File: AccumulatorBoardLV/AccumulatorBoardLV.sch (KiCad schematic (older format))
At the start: 39 parts, among them J1 BMS Connector 1, J10 Contactor 2, J11 IMD LV, J12 Temperature Board, J13 Energy Meter, J14 Energy Meter, J15 12V from DCDC, J16 HV Interlock, J18 Charger LV, J19 Lid Interlock, J2 BMS Connector 2, J3 BMS TX, J4 BMS RX, J5 BMS Reset, J7 IMD Reset, J8 Temp Reset, J9 Contactor 1, P3 Charger Interlock, U13 DK1A1B-12V, U14 DK1A1B-12V, U15 DK1A1B-12V, U17 G5RL-K1A-E, U18 G5RL-K1A-E, U19 G5RL-K1A-E, U6 L78S05CV-DG, U8 LM555N

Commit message: Clean up LV accumulator schematic
Need to solidify connections between accumulator LV board and temp board
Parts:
- removed J12: Temperature Board, symbol CONN_01X06
- added J?: Current Sensor, symbol CONN_01X03
- added P?: To Temp Board, symbol CONN_01X08
- J?: renamed from P?; value CONN_01X14 -> To ECU
- renumbered P3 to J?
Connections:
- net labels added: AIRS_FINAL_CHARGER
- net labels removed: AIRS_LID_OUT, CUR_SIG
- no-connect marks 2 -> 3
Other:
- moved on the sheet: C1, C?, H1, R10, R11, R12, R8, R9, U13, U14, U15, U6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

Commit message: Add connections to temp board for isolation and fault feedback
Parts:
- removed R10: 2.5kR, symbol R
- removed R8: 3.5kR, symbol R
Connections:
- net labels added: BMS_FLT_LATCHED, IMD_FLT_LATCHED, TEMP_FLT_LATCHED
- wire segments 28 -> 30
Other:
- moved on the sheet: C?, U6
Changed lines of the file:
@@
 LIBS:valves
 LIBS:arduino
-LIBS:AccumulatorBoardLV-cache
 EELAYER 25 0
 EELAYER END
@@
 L L78S05CV-DG U6
 U 1 1 58ABDAE7
-P 2900 6900
-F 0 "U6" H 2700 6800 50  0000 C CNN
-F 1 "L78S05CV-DG" H 2650 7100 50  0000 L CNN
-F 2 "Power_Integrations:TO-220" H 2900 6550 50  0001 C CIN
-F 3 "" H 2900 6900 50  0000 C CNN
-	1    2900 6900
-	1    0    0    -1
-$EndComp
-Text Label 2900 7150 3    60   ~ 0
+P 2800 5600
+F 0 "U6" H 2600 5500 50  0000 C CNN
+F 1 "L78S05CV-DG" H 2550 5800 50  0000 L CNN
+F 2 "Power_Integrations:TO-220" H 2800 5250 50  0001 C CIN
+F 3 "" H 2800 5600 50  0000 C CNN
+	1    2800 5600
+	1    0    0    -1
+$EndComp
+Text Label 2800 5850 3    60   ~ 0
 GND
 $Comp
@@
 L +5V #PWR02
 U 1 1 58B23863
-P 3300 6850
-F 0 "#PWR02" H 3300 6700 50  0001 C CNN
-F 1 "+5V" H 3300 6990 50  0000 C CNN
-F 2 "" H 3300 6850 50  0000 C CNN
-F 3 "" H 3300 6850 50  0000 C CNN
-	1    3300 6850
+P 3200 5550
+F 0 "#PWR02" H 3200 5400 50  0001 C CNN
+F 1 "+5V" H 3200 5690 50  0000 C CNN
+F 2 "" H 3200 5550 50  0000 C CNN
+F 3 "" H 3200 5550 50  0000 C CNN
+	1    3200 5550
 	1    0    0    -1
 $EndComp
@@
 L +12V #PWR017
 U 1 1 58B2EAED
-P 2500 6850
-F 0 "#PWR017" H 2500 6700 50  0001 C CNN
-F 1 "+12V" H 2500 6990 50  0000 C CNN
-F 2 "" H 2500 6850 50  0000 C CNN
-F 3 "" H 2500 6850 50  0000 C CNN
-	1    2500 6850
+P 2400 5550
+F 0 "#PWR017" H 2400 5400 50  0001 C CNN
+F 1 "+12V" H 2400 5690 50  0000 C CNN
+F 2 "" H 2400 5550 50  0000 C CNN
+F 3 "" H 2400 5550 50  0000 C CNN
+	1    2400 5550
 	1    0    0    -1
 $EndComp
@@
 Text Label 6400 3550 2    60   ~ 0
 TEMP_FLT
-Text Label 6900 1800 2    60   ~ 0
-BMS_FLT
 Text Label 6900 2100 2    60   ~ 0
 IMD_FLT
@@
 	1    0    0    -1
 $EndComp
-$Comp
-L R R8
-U 1 1 58B6CCA1
-P 7050 1800
-F 0 "R8" V 7130 1800 50  0000 C CNN
-F 1 "3.5kR" V 7050 1800 50  0000 C CNN
-F 2 "" V 6980 1800 50  0001 C CNN
-F 3 "" H 7050 1800 50  0000 C CNN
-	1    7050 1800
-	0    1    1    0
-$EndComp
-$Comp
-L R R10
-U 1 1 58B6D248
-P 7200 1650
-F 0 "R10" V 7280 1650 50  0000 C CNN
-F 1 "2.5kR" V 7200 1650 50  0000 C CNN
-F 2 "" V 7130 1650 50  0001 C CNN
-F 3 "" H 7200 1650 50  0000 C CNN
-	1    7200 1650
-	1    0    0    -1
-$EndComp
-$Comp
-L GND #PWR035
-U 1 1 58B6D770
-P 7200 1500
-F 0 "#PWR035" H 7200 1250 50  0001 C CNN
-F 1 "GND" H 7200 1350 50  0000 C CNN
-F 2 "" H 7200 1500 50  0000 C CNN
-F 3 "" H 7200 1500 50  0000 C CNN
-	1    7200 1500
-	0    -1   -1   0
-$EndComp
 Text Label 9450 5150 2    60   ~ 0
 IMD_FLT_H
@@
 NoConn ~ 1100 2400
 Wire Wire Line
-	7200 1800 7500 1800
-Wire Wire Line
 	7200 2100 7500 2100
-Text Label 7500 1800 0    60   ~ 0
-BMS_FLT_5
 Text Label 7500 2100 0    60   ~ 0
 IMD_FLT_5
@@
 L GND #PWR?
 U 1 1 595AA8FC
-P 2500 7150
-F 0 "#PWR?" H 2500 6900 50  0001 C CNN
-F 1 "GND" H 2500 7000 50  0000 C CNN
-F 2 "" H 2500 7150 50  0001 C CNN
-F 3 "" H 2500 7150 50  0001 C CNN
-	1    2500 7150
+P 2400 5850
+F 0 "#PWR?" H 2400 5600 50  0001 C CNN
+F 1 "GND" H 2400 5700 50  0000 C CNN
+F 2 "" H 2400 5850 50  0001 C CNN
+F 3 "" H 2400 5850 50  0001 C CNN
+	1    2400 5850
 	1    0    0    -1
 $EndComp
@@
 L CP C?
 U 1 1 595AB32A
-P 3300 7000
-F 0 "C?" H 3325 7100 50  0000 L CNN
-F 1 "0.1uF" H 3325 6900 50  0000 L CNN
-F 2 "" H 3338 6850 50  0001 C CNN
-F 3 "" H 3300 7000 50  0001 C CNN
-	1    3300 7000
+P 3200 5700
+F 0 "C?" H 3225 5800 50  0000 L CNN
+F 1 "0.1uF" H 3225 5600 50  0000 L CNN
+F 2 "" H 3238 5550 50  0001 C CNN
+F 3 "" H 3200 5700 50  0001 C CNN
+	1    3200 5700
 	1    0    0    -1
 $EndComp
@@
 L C C?
 U 1 1 595AB43E
-P 2500 7000
-F 0 "C?" H 2525 7100 50  0000 L CNN
-F 1 "0.47uF" H 2525 6900 50  0000 L CNN
-F 2 "" H 2538 6850 50  0001 C CNN
-F 3 "" H 2500 7000 50  0001 C CNN
-	1    2500 7000
+P 2400 5700
+F 0 "C?" H 2425 5800 50  0000 L CNN
+F 1 "0.47uF" H 2425 5600 50  0000 L CNN
+F 2 "" H 2438 5550 50  0001 C CNN
+F 3 "" H 2400 5700 50  0001 C CNN
+	1    2400 5700
 	1    0    0    -1
 $EndComp
@@
 L GND #PWR?
 U 1 1 595AB92B
-P 3300 7150
-F 0 "#PWR?" H 3300 6900 50  0001 C CNN
-F 1 "GND" H 3300 7000 50  0000 C CNN
-F 2 "" H 3300 7150 50  0001 C CNN
-F 3 "" H 3300 7150 50  0001 C CNN
-	1    3300 7150
+P 3200 5850
+F 0 "#PWR?" H 3200 5600 50  0001 C CNN
+F 1 "GND" H 3200 5700 50  0000 C CNN
+F 2 "" H 3200 5850 50  0001 C CNN
+F 3 "" H 3200 5850 50  0001 C CNN
+	1    3200 5850
 	1    0    0    -1
 $EndComp
@@
 5V_BMS
 Wire Wire Line
-	2500 7150 3300 7150
-Connection ~ 2900 7150
+	2400 5850 3200 5850
+Connection ~ 2800 5850
 Text Label 5050 1100 3    60   ~ 0
 SIG_CURRENT
@@
 NoConn ~ 1100 3350
 NoConn ~ -1800 4150
+$Comp
+L GND #PWR?
+U 1 1 59A4B84E
+P 10800 2100
+F 0 "#PWR?" H 10800 1850 50  0001 C CNN
+F 1 "GND" H 10800 1950 50  0000 C CNN
+F 2 "" H 10800 2100 50  0000 C CNN
+F 3 "" H 10800 2100 50  0000 C CNN
+	1    10800 2100
+	1    0    0    -1
+$EndComp
+$Comp
+L GND #PWR?
+U 1 1 59A4B8D4
+P 10800 3450
+F 0 "#PWR?" H 10800 3200 50  0001 C CNN
+F 1 "GND" H 10800 3300 50  0000 C CNN
+F 2 "" H 10800 3450 50  0000 C CNN
+F 3 "" H 10800 3450 50  0000 C CNN
+	1    10800 3450
+	1    0    0    -1
+$EndComp
+$Comp
+L GND #PWR?
+U 1 1 59A4B95A
+P 10800 4850
+F 0 "#PWR?" H 10800 4600 50  0001 C CNN
+F 1 "GND" H 10800 4700 50  0000 C CNN
+F 2 "" H 10800 4850 50  0000 C CNN
+F 3 "" H 10800 4850 50  0000 C CNN
+	1    10800 4850
+	1    0    0    -1
+$EndComp
+Text Label 10800 700  2    60   ~ 0
+BMS_FLT_LATCHED
+Text Label 10800 2550 2    60   ~ 0
+TEMP_FLT_LATCHED
+Text Label 10800 3950 2    60   ~ 0
+IMD_FLT_LATCHED
+Wire Wire Line
+	10800 1500 10800 700
+Wire Wire Line
+	10800 2850 10800 2550
+Wire Wire Line
+	10800 3950 10800 4250
 $EndSCHEMATC

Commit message: Progress on PE LV and HV boards
Upgraded to Kicad 4.0.7
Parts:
- J1, J13, J14: symbol CONN_01X04 -> Conn_01x04
- J10, J15, J16, J19, J3, J4, J5, J7, J8, J9, J?: symbol CONN_01X02 -> Conn_01x02
- J11: symbol CONN_01X06 -> Conn_01x06
- J18, P?: symbol CONN_01X08 -> Conn_01x08
- J2: symbol CONN_01X12 -> Conn_01x12
- J?: symbol CONN_01X14 -> Conn_01x14
- J?: symbol CONN_01X03 -> Conn_01x03

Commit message: Hopefully finalize PCB schematics
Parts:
- removed J13, J14: Energy Meter, symbol Conn_01x04
- removed J15: 12V from DCDC, Connectors_Molex:Molex_NanoFit_1x02x2.50mm_Straight, symbol Conn_01x02
- removed P?: To Temp Board, symbol Conn_01x08
- added J?: To HV Board, symbol Conn_01x03
- added J?: To Temp Board, symbol Conn_01x10
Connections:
- net labels removed: BMS_FLT_5, EM_COMM+, EM_COMM-
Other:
- moved on the sheet: J16, J?
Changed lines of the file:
@@
 L Conn_01x02 J16
 U 1 1 58A9F1D8
-P 900 5750
-F 0 "J16" H 900 5900 50  0000 C CNN
-F 1 "HV Interlock" V 1000 5750 50  0000 C CNN
-F 2 "Connectors_Molex:Molex_NanoFit_1x02x2.50mm_Straight" H 900 5750 50  0001 C CNN
-F 3 "" H 900 5750 50  0000 C CNN
-	1    900  5750
+P 900 4550
+F 0 "J16" H 900 4700 50  0000 C CNN
+F 1 "HV Interlock" V 1000 4550 50  0000 C CNN
+F 2 "Connectors_Molex:Molex_NanoFit_1x02x2.50mm_Straight" H 900 4550 50  0001 C CNN
+F 3 "" H 900 4550 50  0000 C CNN
+	1    900  4550
 	-1   0    0    -1
 $EndComp
-Text Label 1100 5850 0    60   ~ 0
+Text Label 1100 4650 0    60   ~ 0
 AIRS_FINAL_OUT
 $Comp
@@
 Text Label 8900 4300 2    60   ~ 0
 IMD_FLT_H
-$Comp
-L Conn_01x02 J15
-U 1 1 58B9D04E
-P 900 5050
-F 0 "J15" H 900 5200 50  0000 C CNN
-F 1 "12V from DCDC" V 1000 5050 50  0000 C CNN
-F 2 "Connectors_Molex:Molex_NanoFit_1x02x2.50mm_Straight" H 900 5050 50  0001 C CNN
-F 3 "" H 900 5050 50  0000 C CNN
-	1    900  5050
-	-1   0    0    -1
-$EndComp
-Text Label 1100 5050 0    60   ~ 0
+Text Label 1100 3850 0    60   ~ 0
 12V_SRC
-Text Label 1100 5150 0    60   ~ 0
+Text Label 1100 3950 0    60   ~ 0
 GND
 $Comp
@@
 Text Label 7400 6050 0    60   ~ 0
 TEMP_RESET
-Text Label 1100 2650 0    60   ~ 0
+Text Label 1100 2750 0    60   ~ 0
 5V
-Text Label 1100 2750 0    60   ~ 0
-GND
 Text Label 1100 2850 0    60   ~ 0
+GND
+Text Label 1100 2950 0    60   ~ 0
 CAN_H
-Text Label 1100 2950 0    60   ~ 0
+Text Label 1100 3050 0    60   ~ 0
 CAN_L
 Text Notes 3900 2700 2    60   ~ 0
@@
 Text Label 6200 7250 1    60   ~ 0
 AIRS_CHARGER_IN
-$Comp
-L Conn_01x04 J13
-U 1 1 58DB0ABD
-P 900 3800
-F 0 "J13" H 900 4050 50  0000 C CNN
-F 1 "Energy Meter" V 1000 3800 50  0000 C CNN
-F 2 "" H 900 3800 50  0001 C CNN
-F 3 "" H 900 3800 50  0001 C CNN
-	1    900  3800
-	-1   0    0    -1
-$EndComp
-Text Label 1100 3700 0    60   ~ 0
-12V
-Text Label 1100 3800 0    60   ~ 0
-GND
-Text Label 1100 3900 0    60   ~ 0
-EM_COMM+
-Text Label 1100 4000 0    60   ~ 0
-EM_COMM-
-$Comp
-L Conn_01x04 J14
-U 1 1 58DB261A
-P 900 4400
-F 0 "J14" H 900 4650 50  0000 C CNN
-F 1 "Energy Meter" V 1000 4400 50  0000 C CNN
-F 2 "" H 900 4400 50  0001 C CNN
-F 3 "" H 900 4400 50  0001 C CNN
-	1    900  4400
-	-1   0    0    -1
-$EndComp
-Text Label 1100 4300 0    60   ~ 0
-12V
-Text Label 1100 4400 0    60   ~ 0
-GND
-Text Label 1100 4500 0    60   ~ 0
-EM_COMM+
-Text Label 1100 4600 0    60   ~ 0
-EM_COMM-
 Text Label 5000 3300 0    60   ~ 0
 TIMER
@@
 Connection ~ 9900 4050
 Connection ~ 9700 5150
-Text Label 1100 6550 0    60   ~ 0
+Text Label 1100 5350 0    60   ~ 0
 AIRS_FINAL_CHARGER
 $Comp
 L Conn_01x02 J?
 U 1 1 594F302C
-P 900 6450
-F 0 "J?" H 900 6600 50  0000 C CNN
-F 1 "Charger Interlock" V 1000 6450 50  0000 C CNN
-F 2 "" H 900 6450 50  0001 C CNN
-F 3 "" H 900 6450 50  0000 C CNN
-	1    900  6450
+P 900 5250
+F 0 "J?" H 900 5400 50  0000 C CNN
+F 1 "Charger Interlock" V 1000 5250 50  0000 C CNN
+F 2 "" H 900 5250 50  0001 C CNN
+F 3 "" H 900 5250 50  0000 C CNN
+	1    900  5250
 	-1   0    0    -1
 $EndComp
@@
 Wire Wire Line
 	4350 7250 4350 6850
-Text Label 1100 5750 0    60   ~ 0
+Text Label 1100 4550 0    60   ~ 0
 AIRS_PE_OUT
 $Comp
@@
 Wire Wire Line
 	10700 4850 10700 6100
-Text Label 1100 6450 0    60   ~ 0
+Text Label 1100 5250 0    60   ~ 0
 AIRS_PE_OUT
 $Comp
@@
 Text Label 5150 1100 3    60   ~ 0
 GND
-Text Label 1100 3050 0    60   ~ 0
+Text Label 1100 3150 0    60   ~ 0
 TEMP_FLT
-Text Label 1100 3150 0    60   ~ 0
-IMD_FLT_5
-$Comp
-L Conn_01x08 P?
-U 1 1 59A371CF
-P 900 2950
-F 0 "P?" H 900 3400 50  0000 C CNN
-F 1 "To Temp Board" V 1000 2950 50  0000 C CNN
-F 2 "" H 900 2950 50  0000 C CNN
-F 3 "" H 900 2950 50  0000 C CNN
-	1    900  2950
-	-1   0    0    -1
-$EndComp
 Text Label 1100 3250 0    60   ~ 0
-BMS_FLT_5
-NoConn ~ 1100 3350
+IMD_FLT_LATCHED
+Text Label 1100 3350 0    60   ~ 0
+BMS_FLT_LATCHED
 NoConn ~ -1800 4150
 $Comp
@@
 Wire Wire Line
 	10800 3950 10800 4250
+Text Label 1100 3450 0    60   ~ 0
+TEMP_FLT_LATCHED
+$Comp
+L Conn_01x03 J?
+U 1 1 59B3A48A
+P 900 3950
+F 0 "J?" H 900 4150 50  0000 C CNN
+F 1 "To HV Board" V 1000 3950 50  0000 C CNN
+F 2 "" H 900 3950 50  0001 C CNN
+F 3 "" H 900 3950 50  0001 C CNN
+	1    900  3950
+	-1   0    0    -1
+$EndComp
+Text Label 1100 4050 0    60   ~ 0
+AIRS_FINAL_CHARGER
+Entry Wire Line
+	-550 5500 -450 5600
+$Comp
+L Conn_01x10 J?
+U 1 1 59B3D6DB
+P 900 3050
+F 0 "J?" H 900 3550 50  0000 C CNN
+F 1 "To Temp Board" V 1000 3050 50  0000 C CNN
+F 2 "" H 900 3050 50  0001 C CNN
+F 3 "" H 900 3050 50  0001 C CNN
+	1    900  3050
+	-1   0    0    -1
+$EndComp
+Text Label 1100 2650 0    60   ~ 0
+12V
+NoConn ~ 1100 3550
+Text Label 2400 5550 2    60   ~ 0
+12V
+Text Label 3200 5550 0    60   ~ 0
+5V
 $EndSCHEMATC

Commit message: Merge Temperature board with Accumulator boards
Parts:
- added C? (x2): C, symbol C
- added J?: From HV Board, symbol Conn_01x02
- added J?: Chip 1, symbol Conn_01x08
- added J?: Chip 3, symbol Conn_01x08
- added J?: Chip 2, symbol Conn_01x08
- added J?: Chip 4, symbol Conn_01x08
- added SPI_ISLTR?: ADUM4154ARIZ, symbol ADUM4154ARIZ
- added U?: stm_nucleo_FK303K8, arduino:arduino_mini, symbol stm_nucleo_FK303K8
- added U?: ISO1050, SMD_Packages:DIP-8_SMD, symbol ISO1050
- added U? (x4): MCP3008, symbol MCP3008
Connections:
- net labels added: +3.3V, 3.3V, 3.3V_HV, BATT-, SCLK, TEMP_SCLK, TEMP_SSI, TEMP_SSO, TEMP_SS_0, TEMP_SS_1, TEMP_SS_2, TEMP_SS_3
- wire segments 30 -> 62
- no-connect marks 3 -> 6
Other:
- note added: "LV HV"
- note added: "Temp System"
- moved on the sheet: C1, C?, H1, J1, J18, J19, J2, J3, J4, J5, J7, J8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

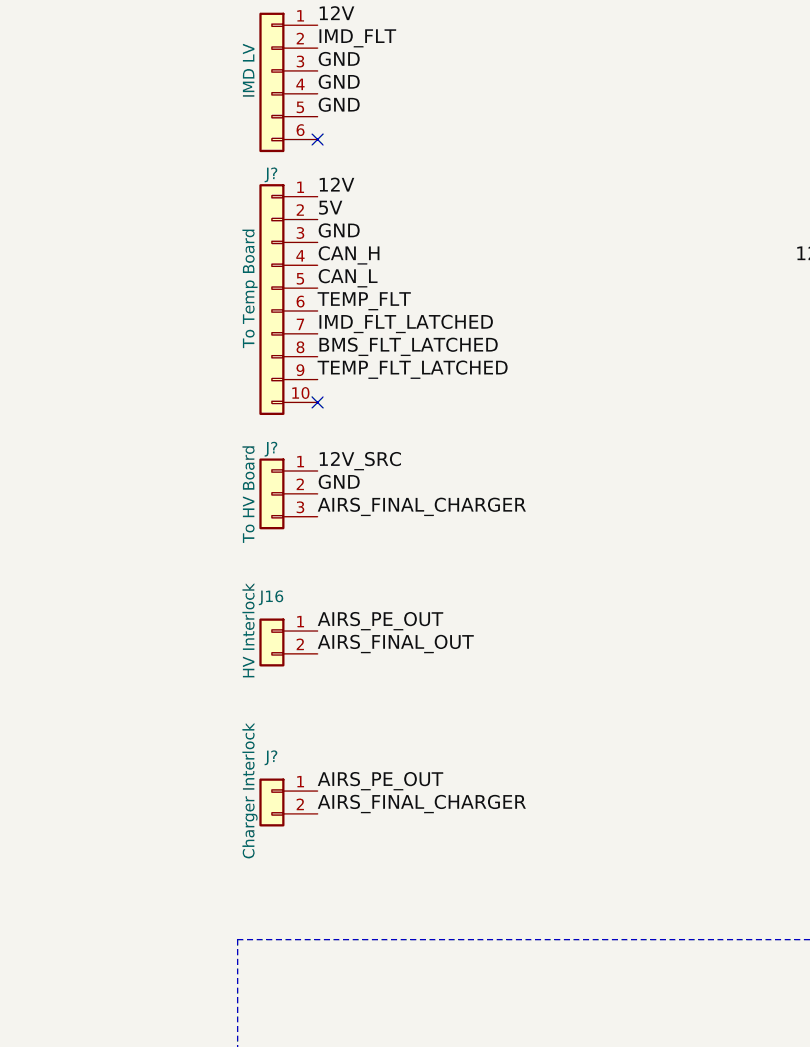
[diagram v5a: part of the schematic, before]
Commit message: Fix the connectors between HV and LV boards
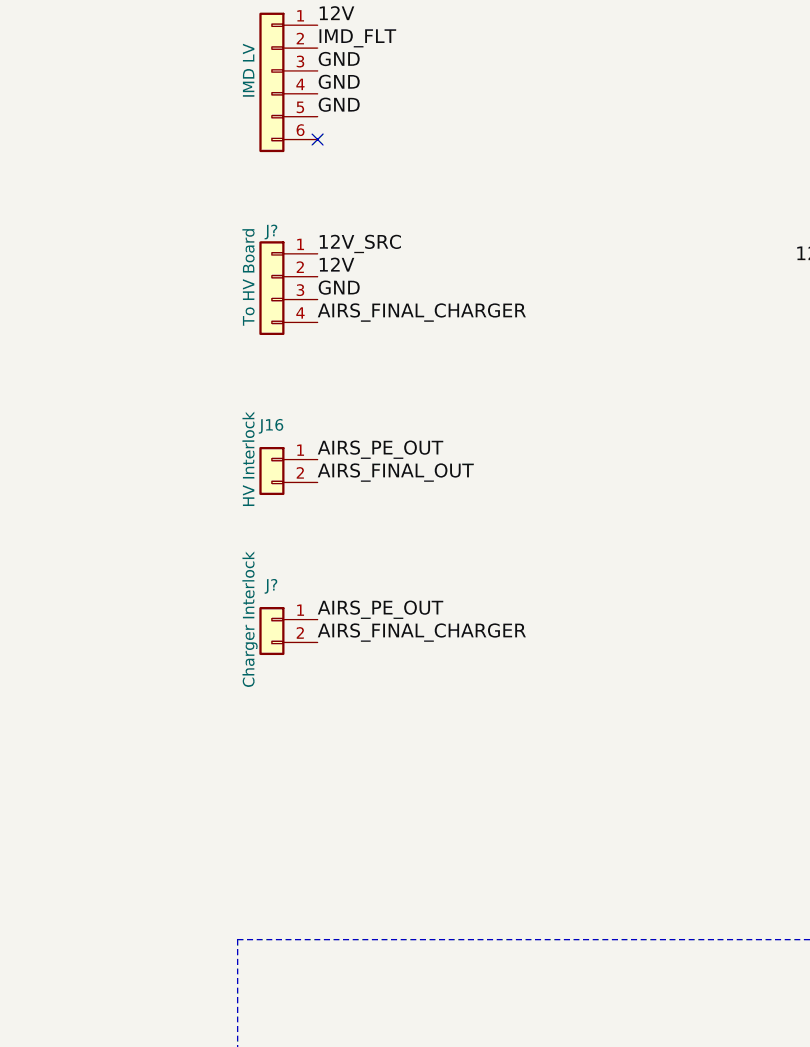
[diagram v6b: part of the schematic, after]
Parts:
- removed J?: To HV Board, symbol Conn_01x03
- removed J?: To Temp Board, symbol Conn_01x10
- added J?: To HV Board, symbol Conn_01x04
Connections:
- no-connect marks 6 -> 5
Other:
- moved on the sheet: J16, J?
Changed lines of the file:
@@
 L Conn_01x02 J16
 U 1 1 58A9F1D8
-P 900 4550
-F 0 "J16" H 900 4700 50  0000 C CNN
-F 1 "HV Interlock" V 1000 4550 50  0000 C CNN
-F 2 "Connectors_Molex:Molex_NanoFit_1x02x2.50mm_Straight" H 900 4550 50  0001 C CNN
-F 3 "" H 900 4550 50  0000 C CNN
-	1    900  4550
+P 900 3800
+F 0 "J16" H 900 3950 50  0000 C CNN
+F 1 "HV Interlock" V 1000 3800 50  0000 C CNN
+F 2 "Connectors_Molex:Molex_NanoFit_1x02x2.50mm_Straight" H 900 3800 50  0001 C CNN
+F 3 "" H 900 3800 50  0000 C CNN
+	1    900  3800
 	-1   0    0    -1
 $EndComp
-Text Label 1100 4650 0    60   ~ 0
+Text Label 1100 3900 0    60   ~ 0
 AIRS_FINAL_OUT
 $Comp
@@
 Text Label 13750 4350 2    60   ~ 0
 IMD_FLT_H
-Text Label 1100 3850 0    60   ~ 0
+Text Label 1100 2900 0    60   ~ 0
 12V_SRC
-Text Label 1100 3950 0    60   ~ 0
+Text Label 1100 3100 0    60   ~ 0
 GND
 $Comp
@@
 Text Label 8650 4600 0    60   ~ 0
 TEMP_RESET
-Text Label 1100 2750 0    60   ~ 0
-5V
-Text Label 1100 2850 0    60   ~ 0
-GND
-Text Label 1100 2950 0    60   ~ 0
-CAN_H
-Text Label 1100 3050 0    60   ~ 0
-CAN_L
 Text Notes 8650 800  2    60   ~ 0
 Fault Latching Logic
@@
 	1    0    0    -1
 $EndComp
-Text Label 1100 5350 0    60   ~ 0
+Text Label 1100 4600 0    60   ~ 0
 AIRS_FINAL_CHARGER
 $Comp
 L Conn_01x02 J?
 U 1 1 594F302C
-P 900 5250
-F 0 "J?" H 900 5400 50  0000 C CNN
-F 1 "Charger Interlock" V 1000 5250 50  0000 C CNN
-F 2 "" H 900 5250 50  0001 C CNN
-F 3 "" H 900 5250 50  0000 C CNN
-	1    900  5250
+P 900 4500
+F 0 "J?" H 900 4650 50  0000 C CNN
+F 1 "Charger Interlock" V 1000 4500 50  0000 C CNN
+F 2 "" H 900 4500 50  0001 C CNN
+F 3 "" H 900 4500 50  0000 C CNN
+	1    900  4500
 	-1   0    0    -1
 $EndComp
@@
 	-1   0    0    1
 $EndComp
-Text Label 1100 4550 0    60   ~ 0
+Text Label 1100 3800 0    60   ~ 0
 AIRS_PE_OUT
 $Comp
@@
 Text Label 4600 4700 1    60   ~ 0
 AIRS_PE_OUT
-Text Label 1100 5250 0    60   ~ 0
+Text Label 1100 4500 0    60   ~ 0
 AIRS_PE_OUT
 $Comp
@@
 Text Label 5750 1150 3    60   ~ 0
 GND
-Text Label 1100 3150 0    60   ~ 0
-TEMP_FLT
-Text Label 1100 3250 0    60   ~ 0
-IMD_FLT_LATCHED
-Text Label 1100 3350 0    60   ~ 0
-BMS_FLT_LATCHED
 NoConn ~ -1800 4150
 $Comp
@@
 Text Label 15650 4000 2    60   ~ 0
 IMD_FLT_LATCHED
-Text Label 1100 3450 0    60   ~ 0
-TEMP_FLT_LATCHED
-$Comp
-L Conn_01x03 J?
-U 1 1 59B3A48A
-P 900 3950
-F 0 "J?" H 900 4150 50  0000 C CNN
-F 1 "To HV Board" V 1000 3950 50  0000 C CNN
-F 2 "" H 900 3950 50  0001 C CNN
-F 3 "" H 900 3950 50  0001 C CNN
-	1    900  3950
-	-1   0    0    -1
-$EndComp
-Text Label 1100 4050 0    60   ~ 0
+Text Label 1100 3200 0    60   ~ 0
 AIRS_FINAL_CHARGER
 Entry Wire Line
 	-550 5500 -450 5600
-$Comp
-L Conn_01x10 J?
-U 1 1 59B3D6DB
-P 900 3050
-F 0 "J?" H 900 3550 50  0000 C CNN
-F 1 "To Temp Board" V 1000 3050 50  0000 C CNN
-F 2 "" H 900 3050 50  0001 C CNN
-F 3 "" H 900 3050 50  0001 C CNN
-	1    900  3050
-	-1   0    0    -1
-$EndComp
-Text Label 1100 2650 0    60   ~ 0
-12V
-NoConn ~ 1100 3550
 Text Label 3350 2950 2    60   ~ 0
 12V
@@
 Text Label 7250 6250 0    60   ~ 0
 3.3V_HV
+$Comp
+L Conn_01x04 J?
+U 1 1 59EB2CF9
+P 900 3000
+F 0 "J?" H 900 3200 50  0000 C CNN
+F 1 "To HV Board" V 1000 3000 50  0000 C CNN
+F 2 "" H 900 3000 50  0001 C CNN
+F 3 "" H 900 3000 50  0001 C CNN
+	1    900  3000
+	-1   0    0    -1
+$EndComp
+Text Label 1100 3000 0    60   ~ 0
+12V
 $EndSCHEMATC
